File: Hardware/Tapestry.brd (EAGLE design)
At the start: 76.2 x 73.7 mm, 119 parts, among them J1 CORTEX_DEBUGPTH, J10 3.3V, J11 VIN, J12 A4, J13 A5, J2 POWER_JACKPTH_LOCK, J3 AOUT4L, J4 AOUT4R, J5 AOUT5L, J6 AOUT5R, J7 AIN3R, J8 AIN3L, J9 3.3VA, U1 ATSAMS70NXXA-AN, U2 AK4618VQSFE-PACKAGE, U3 LM1117, U4 LM1117, Y1 12MHz

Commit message: Ready for group review.
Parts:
- added SJ3: JUMPER-PAD-2-NC_BY_TRACE, SparkFun-Passives:PAD-JUMPER-2-NC_BY_TRACE_YES_SILK
- moved C12 20.2 mm to (11.2, 38.4), turned to 0 degrees
- moved C33 20.2 mm to (11.2, 39.6), turned to 0 degrees
- moved TP3 5.08 mm to (12.7, 57.1)
- moved C13 3.56 mm to (34.5, 58.7), turned to 270 degrees
- moved C17 3.56 mm to (34.5, 62.2), turned to 90 degrees
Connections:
- net 3.3V: now also C13.1, C16.1, SJ3.1, SJ3.2, U2.39
- net 3.3V_A: no longer C13.1, C16.1, U2.39
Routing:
- net 3.3V: track 222.9 -> 262.7 mm, vias 21 -> 22
- net 3.3V_A: track 69.8 -> 63.9 mm
- net SDCMD: track 81.2 -> 84.9 mm
- net SDCLK: track 52.8 -> 56.3 mm
- net SDD0: track 70.9 -> 73.6 mm
- net SDCD: track 65.1 -> 65.9 mm

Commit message: Updates after Monday morning review.
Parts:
- removed D2: MBRA140, SparkFun-DiscreteSemi:SMA-DIODE
- added LOGO2: OSHW-LOGOM, SparkFun-Aesthetics:OSHW-LOGO-M
- JP1: value USBSMD -> USB-MICROB"; device SparkFun-Connectors:USB-MINIB -> SparkFun-Connectors:USB-B-MICRO-SMD_V03
- moved STANDOFF3 15.2 mm to (57.1, 3.81)
- moved J2 7.62 mm to (76.2, 4.35)
- moved J11 6.35 mm to (58.4, 7.62)
- moved FRAME1 3.81 mm to (-1.27, -31.8)
- moved JP1 3.17 mm to (1.91, 15.2)
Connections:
- removed net N$8: D2.C, D3.A
- net N$7: now also D3.A; no longer D2.A
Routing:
- net VIN: track 39.6 -> 48.9 mm
- net N$7: track 50.4 -> 58.7 mm
- net N$8: track 3.81 -> 0.00 mm
- net NRESET: track 66.6 -> 62.8 mm
- net HSDM: track 32.5 -> 35.5 mm
- net HSDP: track 33.3 -> 36.3 mm

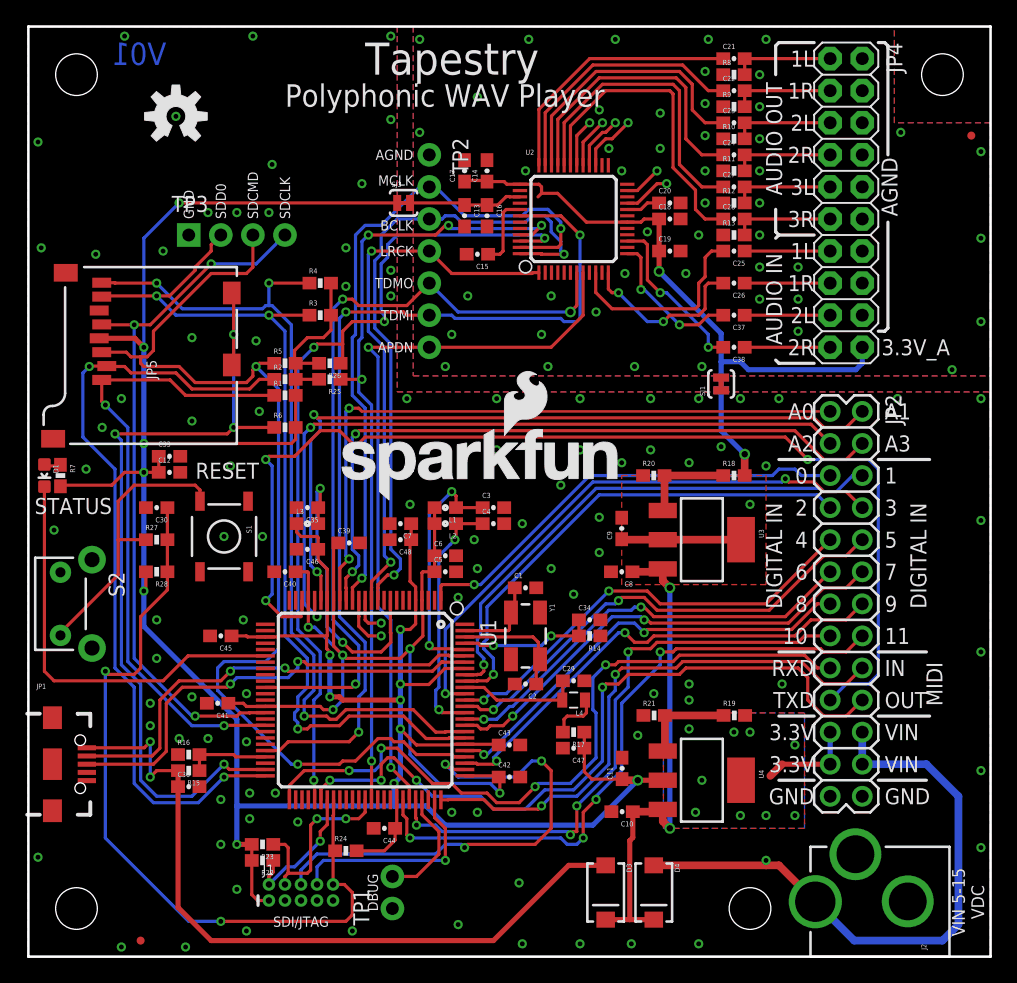
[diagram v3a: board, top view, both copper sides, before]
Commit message: Swapped location of SD socket and reset switches.
Added some more branding to silkscreen.
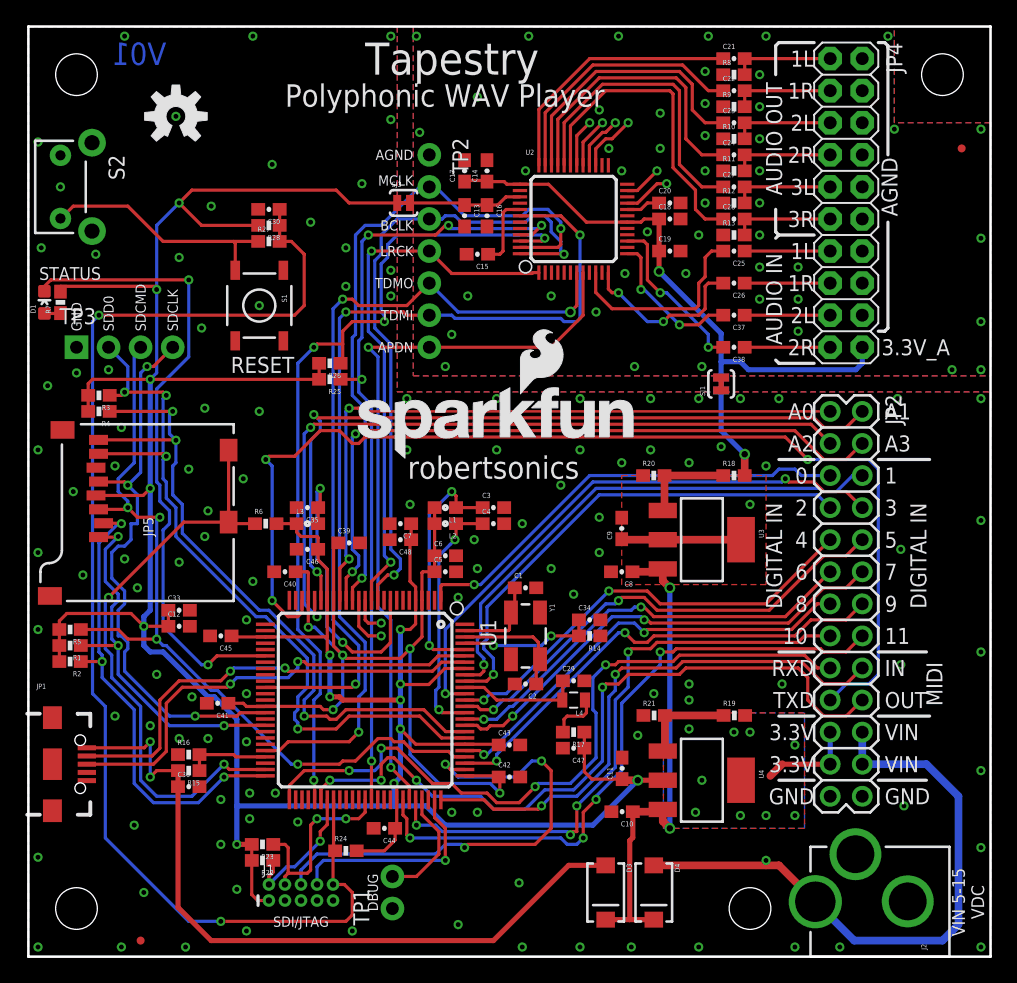
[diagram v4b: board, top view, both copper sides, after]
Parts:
- added LOGO3: SFE_LOGO_NAME.2_INCH, SparkFun-Aesthetics:SFE_LOGO_NAME_.2
- moved S2 33.0 mm to (2.54, 61.0)
- moved R28 28.8 mm to (19.1, 57.9)
- moved R2 28.1 mm to (3.30, 23.4), turned to 180 degrees
- moved R5 27.1 mm to (3.30, 25.9), turned to 180 degrees
- moved R1 26.1 mm to (3.30, 24.6), turned to 180 degrees
- moved C30 25.2 mm to (19.1, 59.2)
- moved R27 25.2 mm to (19.1, 56.6)
- moved R4 20.3 mm to (5.59, 43.2), turned to 180 degrees
- moved R3 18.6 mm to (5.59, 44.5), turned to 180 degrees
- moved S1 18.5 mm to (18.3, 51.6)
- moved D1 13.7 mm to (1.27, 51.8), turned to 0 degrees
- moved R7 13.7 mm to (2.54, 51.8), turned to 90 degrees
- moved TP3 12.6 mm to (3.81, 48.3)
- moved JP5 12.4 mm to (16.3, 28.2)
- moved C33 12.2 mm to (11.9, 27.4)
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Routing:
- net NRESET: track 62.8 -> 100.7 mm
- net SDD3: track 62.5 -> 37.6 mm, vias 2 -> 3
- net SDD2: track 50.3 -> 30.1 mm, vias 2 -> 3
- net SDCMD: track 84.9 -> 65.0 mm, vias 2 -> 4
- net SDCD: track 65.9 -> 47.8 mm, vias 4 -> 2
- net N$10: track 33.3 -> 51.4 mm, vias 0 -> 2
- net 3.3V: track 262.9 -> 276.4 mm
- net SDD1: track 67.6 -> 54.9 mm
- net SDD0: track 73.6 -> 61.5 mm, vias 3 -> 4
- net SDCLK: track 56.3 -> 45.5 mm
- net N$26: track 22.8 -> 19.6 mm
- net TXD: track 88.3 -> 87.4 mm
- net 3.3V_A: track 63.9 -> 63.2 mm
- net GND: vias 142 -> 163
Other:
- board text added: "robertsonics"

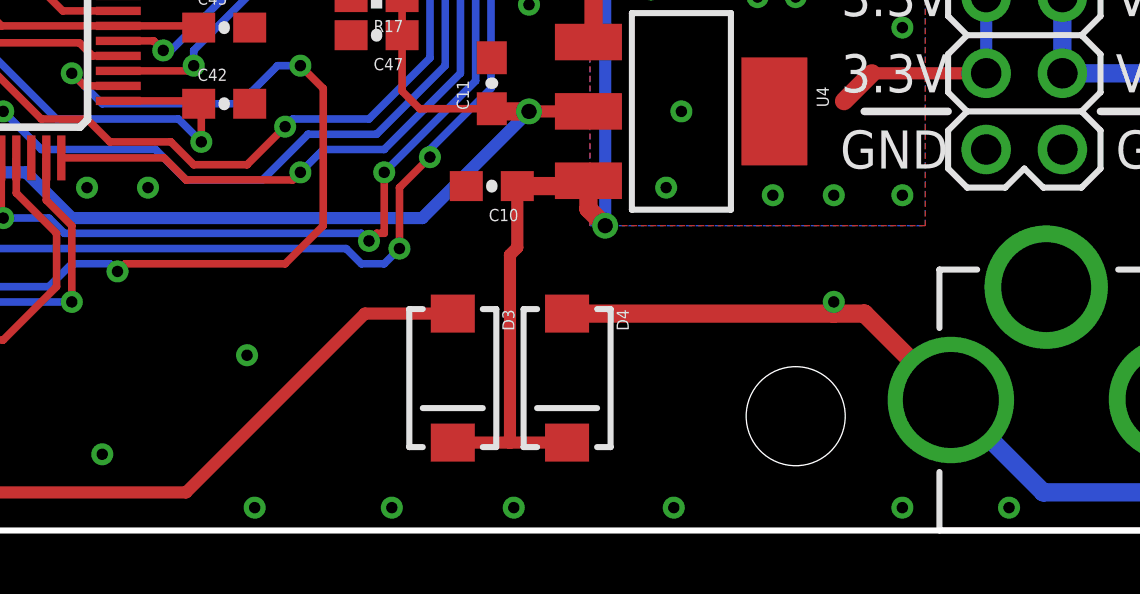
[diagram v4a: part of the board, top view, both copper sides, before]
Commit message: Revising power input.
Using RG Keen's "ideal diode" for barrel input, avoiding a diode drop on
the barrel input, so it's prioritized over Vusb if both are plugged in.
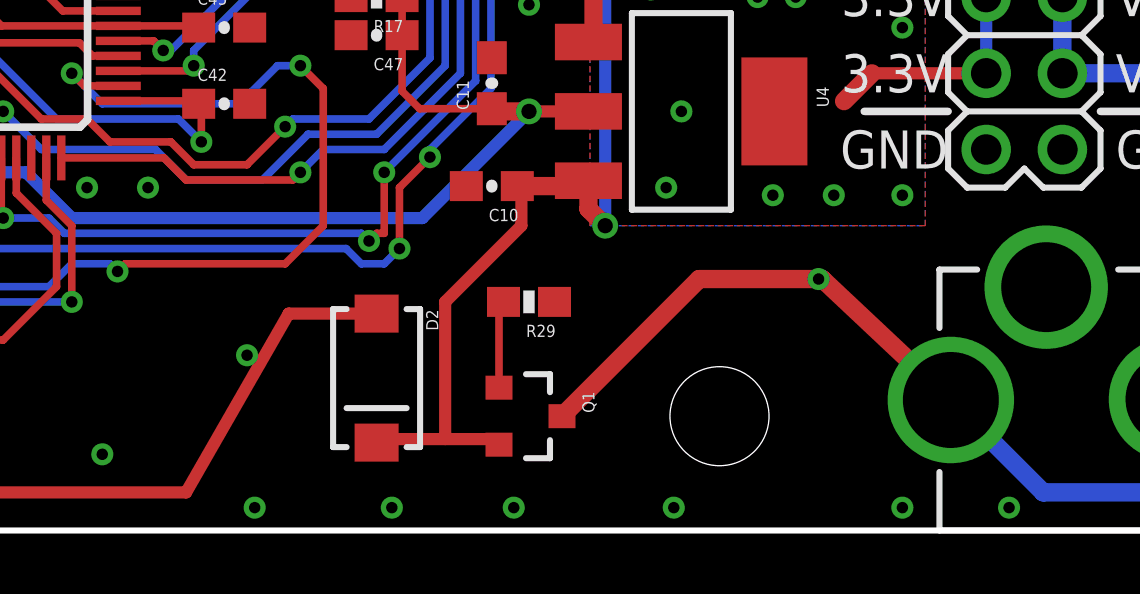
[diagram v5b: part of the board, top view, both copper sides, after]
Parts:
- removed D3, D4: MBRA140, SparkFun-DiscreteSemi:SMA-DIODE
- added D2: MBRA140, SparkFun-DiscreteSemi:SMA-DIODE
- added Q1: 2.5A/30V, SparkFun-DiscreteSemi:SOT23-3
- added R29: 1M, SparkFun-Resistors:0603-RES
- J2: value POWER_JACKPTH_LOCK -> POWER_JACK
- moved STANDOFF3 2.54 mm to (54.6, 3.81)
- moved J11 0.92 mm to (57.9, 8.38)
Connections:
- new net N$75: Q1.1, R29.2
- net GND: now also R29.1
- net N$7: now also D2.A; no longer D3.A
- net N$9: now also D2.C, Q1.2; no longer D3.C, D4.C
- net VIN: now also Q1.3; no longer D4.A
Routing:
- net N$75: track 0.00 -> 2.92 mm
- net VIN: track 48.9 -> 51.0 mm
- net N$7: track 58.7 -> 57.1 mm
- net N$9: track 39.9 -> 41.2 mm

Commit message: Quick DRC fixes.
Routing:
- net N$7: track 57.1 -> 56.1 mm
- net GND: vias 163 -> 166
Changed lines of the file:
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@@
 <setting verticaltext="up"/>
 </settings>
-<grid distance="0.1" unitdist="inch" unit="inch" style="lines" multiple="1" display="yes" altdistance="0.01" altunitdist="inch" altunit="inch"/>
+<grid distance="0.01" unitdist="inch" unit="inch" style="lines" multiple="1" display="yes" altdistance="0.001" altunitdist="inch" altunit="inch"/>
 <layers>
 <layer number="1" name="Top" color="4" fill="1" visible="yes" active="yes"/>
@@
 <layer number="37" name="tTest" color="7" fill="1" visible="no" active="yes"/>
 <layer number="38" name="bTest" color="7" fill="1" visible="no" active="yes"/>
-<layer number="39" name="tKeepout" color="4" fill="11" visible="yes" active="yes"/>
+<layer number="39" name="tKeepout" color="4" fill="11" visible="no" active="yes"/>
 <layer number="40" name="bKeepout" color="1" fill="11" visible="no" active="yes"/>
 <layer number="41" name="tRestrict" color="4" fill="10" visible="no" active="yes"/>
@@
 <via x="9.652" y="18.288" extent="1-16" drill="0.381"/>
 <via x="0.762" y="7.874" extent="1-16" drill="0.381"/>
-<via x="34.036" y="2.54" extent="1-16" drill="0.381"/>
+<via x="32.766" y="0.762" extent="1-16" drill="0.381"/>
 <via x="38.862" y="5.842" extent="1-16" drill="0.381"/>
 <via x="39.116" y="0.762" extent="1-16" drill="0.381"/>
@@
 <via x="6.858" y="38.862" extent="1-16" drill="0.381"/>
 <contactref element="R29" pad="1"/>
+<via x="35.56" y="6.858" extent="1-16" drill="0.381"/>
+<via x="32.766" y="4.318" extent="1-16" drill="0.381"/>
+<via x="37.338" y="3.302" extent="1-16" drill="0.381"/>
 </signal>
 <signal name="N$1">
@@
 <wire x1="11.85" y1="13.462" x2="11.85" y2="3.898" width="0.4064" layer="1"/>
 <wire x1="11.85" y1="3.898" x2="14.478" y2="1.27" width="0.4064" layer="1"/>
-<wire x1="14.478" y1="1.27" x2="36.83" y2="1.27" width="0.4064" layer="1"/>
+<wire x1="14.478" y1="1.27" x2="31.75" y2="1.27" width="0.4064" layer="1"/>
 <via x="9.652" y="17.018" extent="1-16" drill="0.381"/>
 <wire x1="9.652" y1="17.018" x2="9.652" y2="14.224" width="0.254" layer="16"/>
@@
 <wire x1="9.174" y1="16.54" x2="9.652" y2="17.018" width="0.254" layer="1"/>
 <contactref element="D2" pad="A"/>
-<wire x1="43.18" y1="7.23" x2="40.25" y2="7.23" width="0.4064" layer="1"/>
-<wire x1="40.25" y1="7.23" x2="36.83" y2="1.27" width="0.4064" layer="1"/>
+<wire x1="43.18" y1="7.23" x2="37.71" y2="7.23" width="0.4064" layer="1"/>
+<wire x1="31.75" y1="1.27" x2="37.71" y2="7.23" width="0.4064" layer="1"/>
 </signal>
 <signal name="N$9">
@@
 <wire x1="66.04" y1="17.78" x2="66.04" y2="15.24" width="0.6096" layer="16"/>
 <contactref element="J11" pad="P$1"/>
-<wire x1="62.3222" y1="4.35" x2="58.0362" y2="8.382" width="0.6096" layer="1"/>
 <wire x1="66.04" y1="15.24" x2="71.12" y2="15.24" width="0.6096" layer="16"/>
 <wire x1="71.12" y1="15.24" x2="73.66" y2="12.7" width="0.6096" layer="16"/>
@@
 <wire x1="53.932" y1="8.382" x2="57.912" y2="8.382" width="0.6096" layer="1"/>
 <wire x1="58.0362" y1="8.382" x2="57.912" y2="8.382" width="0.6096" layer="1"/>
+<wire x1="62.3222" y1="4.35" x2="58.2902" y2="8.382" width="0.6096" layer="1"/>
+<wire x1="58.2902" y1="8.382" x2="57.912" y2="8.382" width="0.6096" layer="1"/>
 </signal>
 <signal name="N$14">

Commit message: Adding DNS designation to barrel jack.
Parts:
- J2: value POWER_JACK -> POWER_JACK DNS
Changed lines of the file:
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@@
 <setting verticaltext="up"/>
 </settings>
-<grid distance="0.01" unitdist="inch" unit="inch" style="lines" multiple="1" display="yes" altdistance="0.001" altunitdist="inch" altunit="inch"/>
+<grid distance="0.05" unitdist="inch" unit="inch" style="lines" multiple="1" display="yes" altdistance="0.005" altunitdist="inch" altunit="inch"/>
 <layers>
 <layer number="1" name="Top" color="4" fill="1" visible="yes" active="yes"/>
@@
 <layer number="45" name="Holes" color="7" fill="1" visible="yes" active="yes"/>
 <layer number="46" name="Milling" color="3" fill="1" visible="no" active="yes"/>
-<layer number="47" name="Measures" color="7" fill="1" visible="yes" active="yes"/>
+<layer number="47" name="Measures" color="7" fill="1" visible="no" active="yes"/>
 <layer number="48" name="Document" color="7" fill="1" visible="no" active="yes"/>
 <layer number="49" name="Reference" color="7" fill="1" visible="no" active="yes"/>
@@
 </element>
 <element name="LOGO1" library="SparkFun-Aesthetics" package="SFE_LOGO_NAME_FLAME_.2" value="SFE_LOGO_NAME_FLAME.2_INCH" x="25.4" y="39.37"/>
-<element name="J2" library="SparkFun-Connectors" package="POWER_JACK_PTH_LOCK" value="POWER_JACK" x="76.2" y="4.35" rot="R90">
+<element name="J2" library="SparkFun-Connectors" package="POWER_JACK_PTH_LOCK" value="POWER_JACK DNS" x="76.2" y="4.35" rot="R90">
 <attribute name="SF_ID" value="PRT-00119" x="76.2" y="4.35" size="1.778" layer="27" font="vector" ratio="15" rot="R90" display="off"/>
 <attribute name="PROD_ID" value="CONN-08197" x="76.2" y="4.35" size="1.778" layer="27" font="vector" ratio="15" rot="R90" display="off"/>
